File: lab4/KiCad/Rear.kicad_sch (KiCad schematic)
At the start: 44 parts, among them J2 Current test, J20 CAN A isolation, J21 CAN A test, J24 CAN B isolation, J25 CAN B test, J3 Current test, U2 ACS712ELCTR-05B-T, U20 MCP2515T-I/ST, U21 SN65HVD231MDREP, U24 MCP2515T-I/ST, U25 SN65HVD231MDREP, U3 ACS712ELCTR-05B-T, Y20 16 MHz, Y24 16 MHz

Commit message: Integrate Lab 4 MCU support, diagnostics and hierarchical connections
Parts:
- added C600: 100n VDD19, Capacitor_SMD:C_0603_1608Metric, symbol Device:C
- added C601: 100n VDD32, Capacitor_SMD:C_0603_1608Metric, symbol Device:C
- added C602: 100n VDD48, Capacitor_SMD:C_0603_1608Metric, symbol Device:C
- added C603: 100n VDD64, Capacitor_SMD:C_0603_1608Metric, symbol Device:C
- added C604: 100n VBAT, Capacitor_SMD:C_0603_1608Metric, symbol Device:C
- added C605: 4.7u VDD bulk, Capacitor_SMD:C_0805_2012Metric, symbol Device:C
- added C606: 4.7u VCAP1, Capacitor_SMD:C_0805_2012Metric, symbol Device:C
- added C607: 100n VDDA, Capacitor_SMD:C_0603_1608Metric, symbol Device:C
- added C608: 1u VDDA, Capacitor_SMD:C_0603_1608Metric, symbol Device:C
- added C609: 100n NRST, Capacitor_SMD:C_0603_1608Metric, symbol Device:C
- added C610: 100n TEST, Capacitor_SMD:C_0603_1608Metric, symbol Device:C
- added D610: STATUS green, LED_SMD:LED_0603_1608Metric, symbol Device:LED
- added D611: ERR red, LED_SMD:LED_0603_1608Metric, symbol Device:LED
- added D612: DEG_A yellow, LED_SMD:LED_0603_1608Metric, symbol Device:LED
- added D613: DEG_B yellow, LED_SMD:LED_0603_1608Metric, symbol Device:LED
- added FB60: 600R @100MHz, Inductor_SMD:L_0603_1608Metric, symbol Device:FerriteBead
- added J600: BOOT recovery, Connector_PinHeader_2.54mm:PinHeader_1x02_P2.54mm_Vertical, symbol Connector_Generic:Conn_01x02
- added J601: SWD (2.54mm), Connector_PinHeader_2.54mm:PinHeader_1x06_P2.54mm_Vertical, symbol Connector_Generic:Conn_01x06
- added J602: 3.3V TTL UART, Connector_PinHeader_2.54mm:PinHeader_1x03_P2.54mm_Vertical, symbol Connector_Generic:Conn_01x03
- added J603: LAB3 rows 1-13, Connector_PinHeader_2.54mm:PinHeader_1x13_P2.54mm_Vertical, symbol Connector_Generic:Conn_01x13
- added J604: Additional probes, Connector_PinHeader_2.54mm:PinHeader_1x11_P2.54mm_Vertical, symbol Connector_Generic:Conn_01x11
- added J605: Reserved / encoder probes, Connector_PinHeader_2.54mm:PinHeader_1x07_P2.54mm_Vertical, symbol Connector_Generic:Conn_01x07
- added R600: 10k BOOT0, Resistor_SMD:R_0603_1608Metric, symbol Device:R
- added R601: 10k NRST, Resistor_SMD:R_0603_1608Metric, symbol Device:R
- added R602: 10k TEST pullup, Resistor_SMD:R_0603_1608Metric, symbol Device:R
- added R610, R611, R612, R613: 1k, Resistor_SMD:R_0603_1608Metric, symbol Device:R
- added R630, R631, R632, R633, R634, R635: 10k boot pulldown, Resistor_SMD:R_0603_1608Metric, symbol Device:R
- added SW60, SW61: SWT0210-045026GSA, symbol Switch:SW_Push
- added U60: STM32F401RET6TR, Package_QFP:LQFP-64_10x10mm_P0.5mm, symbol MCU_ST_STM32F4:STM32F401RETx
- U20, U24: symbol Interface_CAN_LIN:MCP2515-xST -> Lab4_Logic:MCP2515_TSSOP20
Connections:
- net +3V3: now also C600.1, C601.1, C602.1, C603.1, C604.1, C605.1, FB60.1, J600.1 (Pin_1), J601.1 (Pin_1), R601.1, R602.1, U60.1 (VBAT), U60.19 (VDD), U60.32 (VDD), U60.48 (VDD), U60.64 (VDD)
- net GND: now also C600.2, C601.2, C602.2, C603.2, C604.2, C605.2, C606.2, C607.2, C608.2, C609.2, C610.2, D610.1 (K), D611.1 (K), D612.1 (K), D613.1 (K), J601.3 (Pin_3), J601.6 (Pin_6), J602.3 (Pin_3), J603.1 (Pin_1), J603.2 (Pin_2), J604.1 (Pin_1), J604.2 (Pin_2), J605.1 (Pin_1), J605.2 (Pin_2), R600.2, R630.2, R631.2, R632.2, R633.2, R634.2, R635.2, SW60.2, SW61.2, U60.12 (VSSA), U60.18 (VSS), U60.31 (VSS), U60.47 (VSS), U60.63 (VSS)
- net LEFT_ADC: now also J604.10 (Pin_10), U60.16 (PA2)
- net RIGHT_ADC: now also J604.11 (Pin_11), U60.17 (PA3)
- net R_CS_A: now also U60.58 (PB6)
- net R_CS_B: now also U60.38 (PC7)
- net R_INT_A: now also U60.43 (PA10)
- net R_INT_B: now also U60.57 (PB5)
- net R_MISO: now also U60.22 (PA6)
- net R_MOSI: now also U60.23 (PA7)
- net R_SCK: now also U60.21 (PA5)
- new net R_BOOT0: J600.2 (Pin_2), R600.1, U60.60 (BOOT0)
- new net R_DEG_A_LED: J603.7 (Pin_7), R612.1, U60.26 (PB0)
- new net R_DEG_A_LED_ANODE: D612.2 (A), R612.2
- new net R_DEG_B_LED: J603.8 (Pin_8), R613.1, U60.27 (PB1)
- new net R_DEG_B_LED_ANODE: D613.2 (A), R613.2
- new net R_DIR_A_MARKER: J603.11 (Pin_11), U60.29 (PB10)
- new net R_ERROR_LED: J604.4 (Pin_4), R611.1, U60.8 (PC0)
- new net R_ERROR_LED_ANODE: D611.2 (A), R611.2
- new net R_LEFT_ENABLE_PWM: J603.10 (Pin_10), R630.1, U60.42 (PA9)
- new net R_LEFT_ENC_A: J605.3 (Pin_3), U60.28 (PB2)
- new net R_LEFT_ENC_B: J605.4 (Pin_4), U60.55 (PB3)
- new net R_LEFT_IN1: R632.1, U60.34 (PB13)
- new net R_LEFT_IN2: R633.1, U60.35 (PB14)
- new net R_OVERLOAD_MARKER: J604.9 (Pin_9), U60.52 (PC11)
- new net R_PID_MARKER: J604.7 (Pin_7), U60.40 (PC9)
- new net R_PWM_SET_MARKER: J603.9 (Pin_9), U60.62 (PB9)
- new net R_REAR_LEFT_LED: J603.12 (Pin_12), U60.24 (PC4)
- new net R_REAR_RIGHT_LED: J603.13 (Pin_13), U60.25 (PC5)
- new net R_RELAY_TX_MARKER: J605.7 (Pin_7), U60.37 (PC6)
- new net R_RESET_N: C609.1, J601.5 (Pin_5), R601.2, SW60.1, U60.7 (NRST)
- new net R_RIGHT_ENABLE_PWM: J604.8 (Pin_8), R631.1, U60.59 (PB7)
- new net R_RIGHT_ENC_A: J605.5 (Pin_5), U60.56 (PB4)
- new net R_RIGHT_ENC_B: J605.6 (Pin_6), U60.33 (PB12)
- new net R_RIGHT_IN3: R634.1, U60.36 (PB15)
- new net R_RIGHT_IN4: R635.1, U60.51 (PC10)
- new net R_RX_A_MARKER: J603.3 (Pin_3), U60.10 (PC2)
- new net R_RX_B_MARKER: J603.4 (Pin_4), U60.11 (PC3)
- new net R_SELFTEST_BUTTON: C610.1, J604.3 (Pin_3), R602.2, SW61.1, U60.2 (PC13)
- new net R_STATUS_LED: R610.1, U60.50 (PA15)
- new net R_STATUS_LED_ANODE: D610.2 (A), R610.2
- new net R_STEER_TASK_MARKER: J604.6 (Pin_6), U60.9 (PC1)
- new net R_SWCLK: J601.2 (Pin_2), U60.49 (PA14)
- new net R_SWDIO: J601.4 (Pin_4), U60.46 (PA13)
- new net R_TASK_PROBE: J604.5 (Pin_5), U60.39 (PC8)
- new net R_TX_A_MARKER: J603.5 (Pin_5), U60.14 (PA0)
- new net R_TX_B_MARKER: J603.6 (Pin_6), U60.15 (PA1)
- new net R_UART_CONSOLE_RX: J602.2 (Pin_2), U60.45 (PA12)
- new net R_UART_CONSOLE_TX: J602.1 (Pin_1), U60.44 (PA11)
- new net R_VCAP1: C606.1, U60.30 (VCAP1)
- new net R_VDDA: C607.1, C608.1, FB60.2, U60.13 (VREF+)
- no-connect marks 12 -> 21
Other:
- note added: "Driver integration remains open pending overload/current-limit design. PA9/PB7 are motor enables; low means coast during reset. Motor/encoder connector pin order has not been inferred from cable colors."
- note added: "LAB3 header follows handout p17 top-to-bottom. Two GND pins first. SRV/PWM_OUT probe actual actuator PWM; timing markers remain separate. Physical header position / accessibility will be checked during PCB layout."
- note added: "STM32F401RET6 - independent HSI/PLL, no ST-LINK clock dependency"
- note added: "SWD: pin1 VTref senses target voltage; do not feed a second 3.3V supply. UART header is TX/RX/GND, not RS-232. NRST pulls low to reset. BOOT0 low boots flash; fit recovery shunt only for bootloader recovery."
- note added: "Shared rails and CAN backbone connect through the root sheet. SPI, clocks and reset stay within each zone."
- note added: "TEST: active low on PC13, 10k/100n = 1ms release RC. Firmware must debounce and meet the 10ms local-fault deadline. Reset and self-test are separate buttons."
- note added: "VCAP1 is the INTERNAL regulator output. Only its local capacitor connects here. Keep every 100n beside its VDD pin; keep the VCAP loop short. DS10086 Fig.2 / Fig.18."
- note removed: "HOST INTERFACE (to be integrated with the bare MCU / Pi header) SPI1: PA5=SCK, PA6=MISO, PA7=MOSI; PB6=CS_A; PA10=INT_A; PC7=CS_B; PB5=INT_B. These named nets are LOCAL to this zone. All +3V3 / +5V / GND / CAN backbone nets need hierarchy ports before full-board integration."
- title: Rear zone - CAN and motor current sensing -> Rear zone - integrated logic and interfaces

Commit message: Update Lab 4 circuits, assembly BOMs and measured PCB placement
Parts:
- added C800: 100n 50V, Capacitor_SMD:C_0603_1608Metric, symbol Device:C
- added C801, C803: 100n, Capacitor_SMD:C_0603_1608Metric, symbol Device:C
- added C802: 470u 25V, Capacitor_THT:CP_Radial_D8.0mm_P3.50mm, symbol Device:C
- added D800, D801, D802, D803, D804, D805, D806, D807: SK520B, Diode_SMD:D_SMB, symbol Device:D_Schottky
- added J650: REAR LEFT lamp, Connector_PinHeader_2.54mm:PinHeader_1x02_P2.54mm_Vertical, symbol Connector_Generic:Conn_01x02
- added J651: REAR RIGHT lamp, Connector_PinHeader_2.54mm:PinHeader_1x02_P2.54mm_Vertical, symbol Connector_Generic:Conn_01x02
- added J80: LEFT motor, Connector_Hirose:Hirose_DF63M-2P-3.96DSA_1x02_P3.96mm_Vertical, symbol Connector_Generic:Conn_01x02
- added J81: RIGHT motor, Connector_Hirose:Hirose_DF63M-2P-3.96DSA_1x02_P3.96mm_Vertical, symbol Connector_Generic:Conn_01x02
- added J82: LEFT encoder, Connector_PinHeader_2.54mm:PinHeader_1x04_P2.54mm_Vertical, symbol Connector_Generic:Conn_01x04
- added J83: RIGHT encoder, Connector_PinHeader_2.54mm:PinHeader_1x04_P2.54mm_Vertical, symbol Connector_Generic:Conn_01x04
- added Q650, Q651: MMBT3904, Package_TO_SOT_SMD:SOT-23, symbol Transistor_BJT:MMBT3904
- added R650, R651: 2.2k, Resistor_SMD:R_0603_1608Metric, symbol Device:R
- added R660, R661: 100k, Resistor_SMD:R_0603_1608Metric, symbol Device:R
- added R670, R671: 220R, Resistor_SMD:R_0603_1608Metric, symbol Device:R
- added R800, R801, R802, R803: 100R, Resistor_SMD:R_0603_1608Metric, symbol Device:R
- added R804, R805, R806, R807: 10k, Resistor_SMD:R_0603_1608Metric, symbol Device:R
- added U80: L298N, Package_TO_SOT_THT:TO-220-15_P2.54x5.08mm_StaggerOdd_Lead4.58mm_Vertical, symbol Driver_Motor:L298N
- added U81: SN74LVC14APWR, Package_SO:TSSOP-14_4.4x5mm_P0.65mm, symbol Lab4_Logic:SN74LVC14A_Encoder
- C200, C201, C240, C241: value Cload TBD -> 18p C0G 50V; Design status (none) -> CL=12pF; equal 18pF caps assume 3pF effective stray; tune a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; MPN (none) -> GRM1885C1H180JA01D
- U21, U25: value SN65HVD231MDREP -> SN65HVD231DR; Design status Course Oct 16 substitution; verify exact supplied ordering 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 -> TI verified SOIC-8 order code; confirm course-stock equival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; MPN SN65HVD231MDREP -> SN65HVD231DR
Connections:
- net +3V3: now also C803.1, R804.1, R805.1, R806.1, R807.1, U81.14 (VCC)
- net +5V: now also C801.1, J82.1 (Pin_1), J83.1 (Pin_1), R670.1, R671.1, U80.9 (Vss)
- net GND: now also C800.2, C801.2, C802.2, C803.2, D801.2 (A), D803.2 (A), D805.2 (A), D807.2 (A), J82.2 (Pin_2), J83.2 (Pin_2), Q650.2 (E), Q651.2 (E), R660.2, R661.2, U80.1 (SENSE_A), U80.15 (SENSE_B), U80.8 (GND), U81.11 (5A), U81.13 (6A), U81.7 (GND)
- net LEFT_BRIDGE: now also D800.2 (A), D801.1 (K), U80.2 (OUT1)
- net LEFT_MOTOR: now also J80.1 (Pin_1)
- net RIGHT_BRIDGE: now also D804.2 (A), D805.1 (K), U80.13 (OUT3)
- net RIGHT_MOTOR: now also J81.1 (Pin_1)
- net R_LEFT_ENABLE_PWM: now also U80.6 (EnA)
- net R_LEFT_ENC_A: now also U81.2 (1Y)
- net R_LEFT_ENC_B: now also U81.4 (2Y)
- net R_LEFT_IN1: now also U80.5 (IN1)
- net R_LEFT_IN2: now also U80.7 (IN2)
- net R_REAR_LEFT_LED: now also R650.1
- net R_REAR_RIGHT_LED: now also R651.1
- net R_RIGHT_ENABLE_PWM: now also U80.11 (EnB)
- net R_RIGHT_ENC_A: now also U81.6 (3Y)
- net R_RIGHT_ENC_B: now also U81.8 (4Y)
- net R_RIGHT_IN3: now also U80.10 (IN3)
- net R_RIGHT_IN4: now also U80.12 (IN4)
- new net LEFT_ENC_A_IN: R800.2, U81.1 (1A)
- new net LEFT_ENC_A_RAW: J82.3 (Pin_3), R800.1, R804.2
- new net LEFT_ENC_B_IN: R801.2, U81.3 (2A)
- new net LEFT_ENC_B_RAW: J82.4 (Pin_4), R801.1, R805.2
- new net LEFT_RETURN: D802.2 (A), D803.1 (K), J80.2 (Pin_2), U80.3 (OUT2)
- new net RIGHT_ENC_A_IN: R802.2, U81.5 (3A)
- new net RIGHT_ENC_A_RAW: J83.3 (Pin_3), R802.1, R806.2
- new net RIGHT_ENC_B_IN: R803.2, U81.9 (4A)
- new net RIGHT_ENC_B_RAW: J83.4 (Pin_4), R803.1, R807.2
- new net RIGHT_RETURN: D806.2 (A), D807.1 (K), J81.2 (Pin_2), U80.14 (OUT4)
- new net R_REAR_LEFT_LED_BASE: Q650.1 (B), R650.2, R660.1
- new net R_REAR_LEFT_LED_PLUS: J650.1 (Pin_1), R670.2
- new net R_REAR_LEFT_LED_SINK: J650.2 (Pin_2), Q650.3 (C)
- new net R_REAR_RIGHT_LED_BASE: Q651.1 (B), R651.2, R661.1
- new net R_REAR_RIGHT_LED_PLUS: J651.1 (Pin_1), R671.2
- new net R_REAR_RIGHT_LED_SINK: J651.2 (Pin_2), Q651.3 (C)
- new net VBAT_PROTECTED: C800.1, C802.1, D800.1 (K), D802.1 (K), D804.1 (K), D806.1 (K), U80.4 (Vs)
- no-connect marks 21 -> 23
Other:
- note added: "ENCODER INPUTS: board pins 1=5.1V, 2=GND, 3=A, 4=B. Verify actual cable order. 10k pullups support open-collector outputs; push-pull input must stay <=5.5V. U81 at 3.3V gives Schmitt hysteresis and MCU-safe outputs; unused inputs grounded. Both A and B invert. Check direction/counts after the PCB firmware port."
- note added: "L298 and output circuits are below. Current limiting and heatsink remain unresolved; no motor-power sign-off."
- note added: "MOTOR POWER STAGE - current-limit / heatsink sign-off still required"
- note added: "OUT1/OUT3 -> ACS712 IP+ -> IP- -> motor lead. Other lead -> OUT2/OUT4, NEVER ground. ENA/ENB high + equal direction inputs gives dynamic braking. Enable low gives coast. Existing 10k pulldowns keep enables low during reset. SENSE_A/B return to power ground. This schematic has no autonomous motor-current limiter. A fuse and filtered ADC are not substitutes. Use an agreed current-limit/driver redes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"
- note removed: "Driver integration remains open pending overload/current-limit design. PA9/PB7 are motor enables; low means coast during reset. Motor/encoder connector pin order has not been inferred from cable colors."

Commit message: Prepare Lab 4 review package and align course assembly plan
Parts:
- C202, C203, C204, C242, C243, C244, C3, C5, C6, C8: Design status (none) -> Preliminary; verify before fabrication; MPN (none) -> KGM15AR71C104KT
- C4, C7: Design status (none) -> Preliminary; verify before fabrication; MPN (none) -> GCM1885C2A102FA16D
- D800, D801, D802, D803, D804, D805, D806, D807: Design status External motor clamp; verify supplier exact 5A/200V part an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 -> SMC Diode Solutions 5A/200V SMB; exact MPN appears in cours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
- J2, J21, J25, J3, JP20, JP24, R202, R242, U2, U20, U24, U3: Design status (none) -> Preliminary; verify before fabrication
- Q650, Q651: MPN MMBT3904 -> MMBT3904-7-F
- R200, R201, R240, R241, R3, R4, R6, R7: Design status (none) -> Preliminary; verify before fabrication; MPN (none) -> CRCW060310K0FKEA
- R5, R8: Design status (none) -> Preliminary; verify before fabrication; MPN (none) -> ERJ-3EKF1001V
- SW60, SW61: Design status Electrical circuit placed; exact GCT footprint drawing stil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 -> GCT drawing located (25-Apr-2025); contact-pair/pad geometr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
- U21, U25: Design status TI verified SOIC-8 order code; confirm course-stock equival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 -> Exact MPN appears in course v3 stock list; TI SOIC-8 pinout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
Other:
- note added: "MOTOR POWER STAGE - cooling / stall behavior to verify"
- note added: "OUT1/OUT3 -> ACS712 IP+ -> IP- -> motor lead. Other lead -> OUT2/OUT4, NEVER ground. ENA/ENB high + equal direction inputs gives dynamic braking. Enable low gives coast. Existing 10k pulldowns keep enables low during reset. SENSE_A/B return to power ground. This schematic has no autonomous motor-current limiter. A fuse and filtered ADC are not substitutes. Keep the course L298N; check cooling and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"
- note removed: "MOTOR POWER STAGE - current-limit / heatsink sign-off still required"
- note removed: "OUT1/OUT3 -> ACS712 IP+ -> IP- -> motor lead. Other lead -> OUT2/OUT4, NEVER ground. ENA/ENB high + equal direction inputs gives dynamic braking. Enable low gives coast. Existing 10k pulldowns keep enables low during reset. SENSE_A/B return to power ground. This schematic has no autonomous motor-current limiter. A fuse and filtered ADC are not substitutes. Use an agreed current-limit/driver redes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"

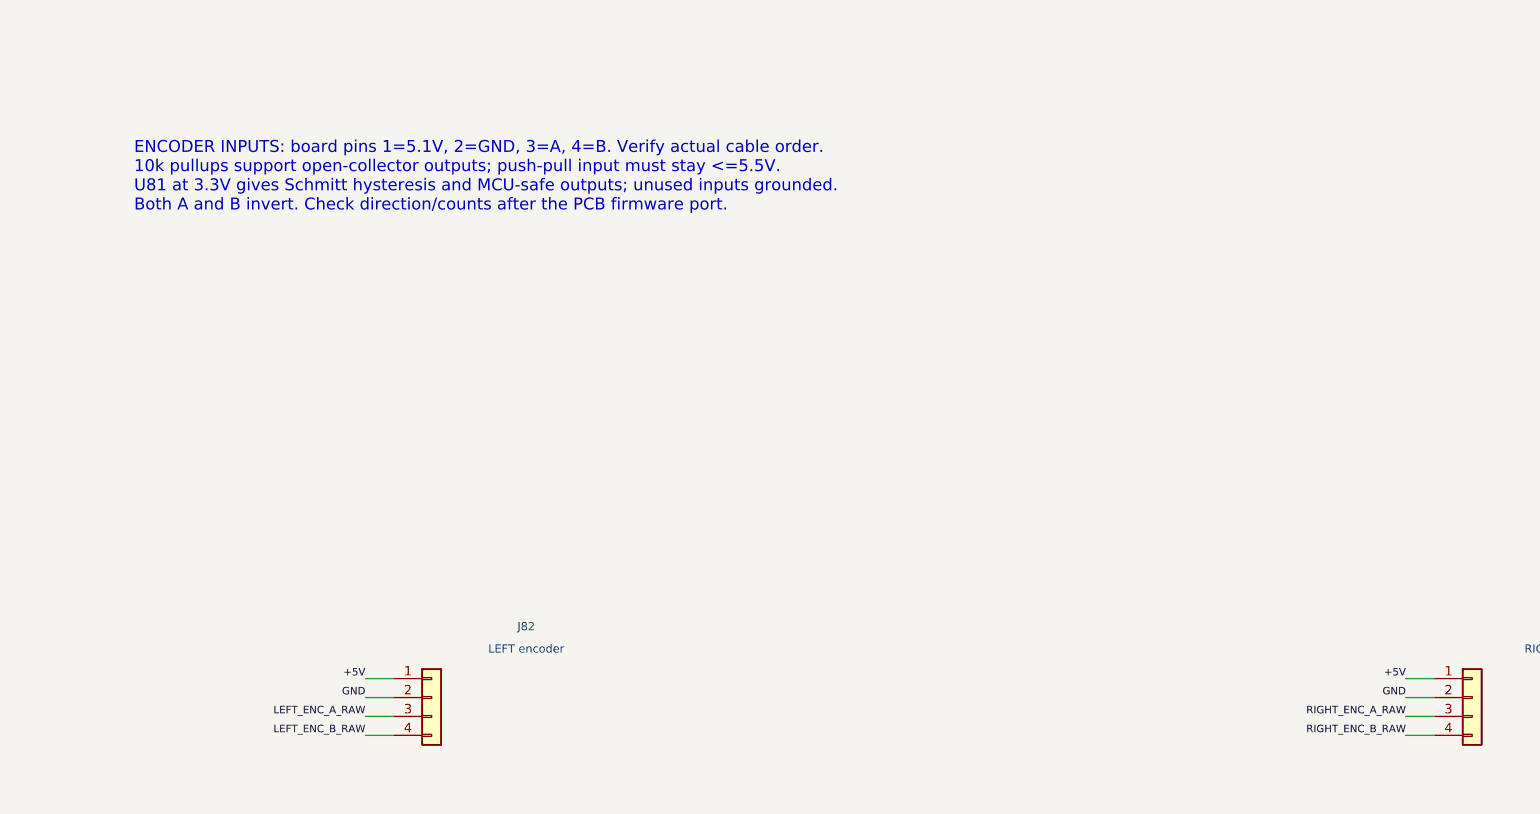
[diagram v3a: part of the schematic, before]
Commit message: Reconcile Lab 4 review schematic, sourcing and verification
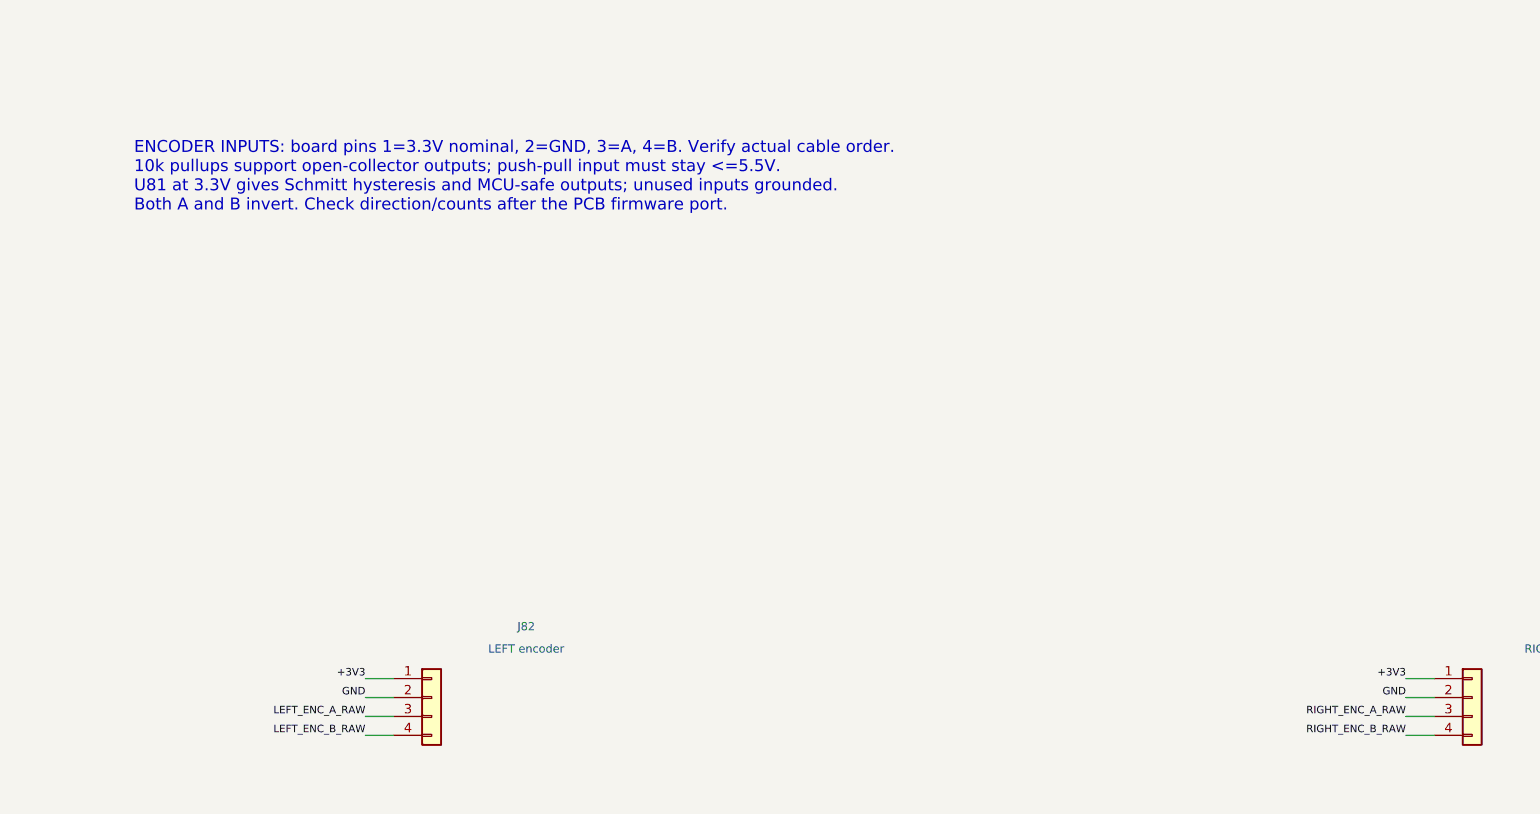
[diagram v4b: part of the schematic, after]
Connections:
- net +3V3: now also J82.1 (Pin_1), J83.1 (Pin_1)
- net +5V: no longer J82.1 (Pin_1), J83.1 (Pin_1)
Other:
- note added: "ENCODER INPUTS: board pins 1=3.3V nominal, 2=GND, 3=A, 4=B. Verify actual cable order. 10k pullups support open-collector outputs; push-pull input must stay <=5.5V. U81 at 3.3V gives Schmitt hysteresis and MCU-safe outputs; unused inputs grounded. Both A and B invert. Check direction/counts after the PCB firmware port."
- note removed: "ENCODER INPUTS: board pins 1=5.1V, 2=GND, 3=A, 4=B. Verify actual cable order. 10k pullups support open-collector outputs; push-pull input must stay <=5.5V. U81 at 3.3V gives Schmitt hysteresis and MCU-safe outputs; unused inputs grounded. Both A and B invert. Check direction/counts after the PCB firmware port."

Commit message: Add verified GCT switch footprints and refresh Lab 4 checks
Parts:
- SW60, SW61: footprint (none) -> Lab4_Switches:GCT_SWT0210_4.5x4.5mm; Design status GCT drawing located (25-Apr-2025); contact-pair/pad geometr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 -> GCT A1 drawing verified: physical terminals 1/2 -> logical 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

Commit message: Apply hole-edge clearance and integrate heatsink and encoder supply
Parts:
- added C804, C805: 10u 16V 10% low-ESR, Capacitor_Tantalum_SMD:CP_EIA-3528-21_Kemet-B, symbol Device:C_Polarized
- added U82: MCP1700-4002E/TO, Package_TO_SOT_THT:TO-92_Inline_Wide, symbol Lab4_Power:MCP1700_4V_TO92
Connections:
- net +3V3: no longer J82.1 (Pin_1), J83.1 (Pin_1)
- net +5V: now also C804.1, U82.2 (VI)
- net GND: now also C804.2, C805.2, U82.1 (GND)
- new net ENC_4V: C805.1, J82.1 (Pin_1), J83.1 (Pin_1), U82.3 (VO)
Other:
- note added: "ENCODER INPUTS: board pins 1=4.0V regulated, 2=GND, 3=A, 4=B. Verify actual cable order. 10k pullups support open-collector outputs; push-pull input must stay <=5.5V. U81 at 3.3V gives Schmitt hysteresis and MCU-safe outputs; unused inputs grounded. Both A and B invert. Check direction/counts after the PCB firmware port."
- note added: "ENCODER SUPPLY: 5.1V -> U82 4.0V -> J82/J83 pin1. 40mA combined planning load, not a measurement. Keep the Schmitt buffer and pullups at3.3V; signal inputs tolerate up to5.5V. C804/C805 are polarized: positive pad1 goes to the named supply."
- note added: "L298 and output circuits are below. Current limiting and motor operating envelope remains unresolved; heatsink geometry is specified; no motor-power sign-off."
- note removed: "ENCODER INPUTS: board pins 1=3.3V nominal, 2=GND, 3=A, 4=B. Verify actual cable order. 10k pullups support open-collector outputs; push-pull input must stay <=5.5V. U81 at 3.3V gives Schmitt hysteresis and MCU-safe outputs; unused inputs grounded. Both A and B invert. Check direction/counts after the PCB firmware port."
- note removed: "L298 and output circuits are below. Current limiting and heatsink remain unresolved; no motor-power sign-off."

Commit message: Correct motor capacitor package and review power and manufacturing margins
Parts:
- C802: footprint Capacitor_THT:CP_Radial_D8.0mm_P3.50mm -> Capacitor_THT:CP_Radial_D10.0mm_P5.00mm

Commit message: Fix L298 drill tolerance and refresh Lab 4 fabrication review
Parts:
- U80: footprint Package_TO_SOT_THT:TO-220-15_P2.54x5.08mm_StaggerOdd_Lead4.58mm_Vertical -> Lab4_Power:ST_L298N_Multiwatt15V_D1.1
